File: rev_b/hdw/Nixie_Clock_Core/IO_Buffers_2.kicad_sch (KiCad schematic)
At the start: 15 parts

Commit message: hid all passive refdes on core PCB
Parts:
- C? (x2): Digi-Key PN (none) -> 1276-2970-1-ND
- C? (x3): Digi-Key PN (none) -> 1276-1935-1-ND
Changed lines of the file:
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@@
       (effects (font (size 1.27 1.27)) (justify right))
     )
-    (property "Digi-Key PN" "" (at 6.35 151.384 0)
+    (property "Digi-Key PN" "1276-2970-1-ND" (at 6.35 151.384 0)
       (effects (font (size 1.27 1.27)) hide)
     )
@@
       (effects (font (size 1.27 1.27)) (justify right))
     )
-    (property "Digi-Key PN" "" (at 149.225 22.86 0)
+    (property "Digi-Key PN" "1276-1935-1-ND" (at 149.225 22.86 0)
       (effects (font (size 1.524 1.524)) hide)
     )
@@
       (effects (font (size 1.27 1.27)) (justify right))
     )
-    (property "Digi-Key PN" "" (at 113.665 22.86 0)
+    (property "Digi-Key PN" "1276-1935-1-ND" (at 113.665 22.86 0)
       (effects (font (size 1.524 1.524)) hide)
     )
@@
       (effects (font (size 1.27 1.27)) (justify right))
     )
-    (property "Digi-Key PN" "" (at 64.135 128.27 0)
+    (property "Digi-Key PN" "1276-1935-1-ND" (at 64.135 128.27 0)
       (effects (font (size 1.524 1.524)) hide)
     )
@@
       (effects (font (size 1.27 1.27)) (justify right))
     )
-    (property "Digi-Key PN" "" (at -29.21 151.384 0)
-      (effects (font (size 1.27 1.27)) hide)
-    )
+    (property "Digi-Key PN" "1276-2970-1-ND" (at -29.21 151.384 0)
+      (effects (font (size 1.27 1.27)) hide)
+    )

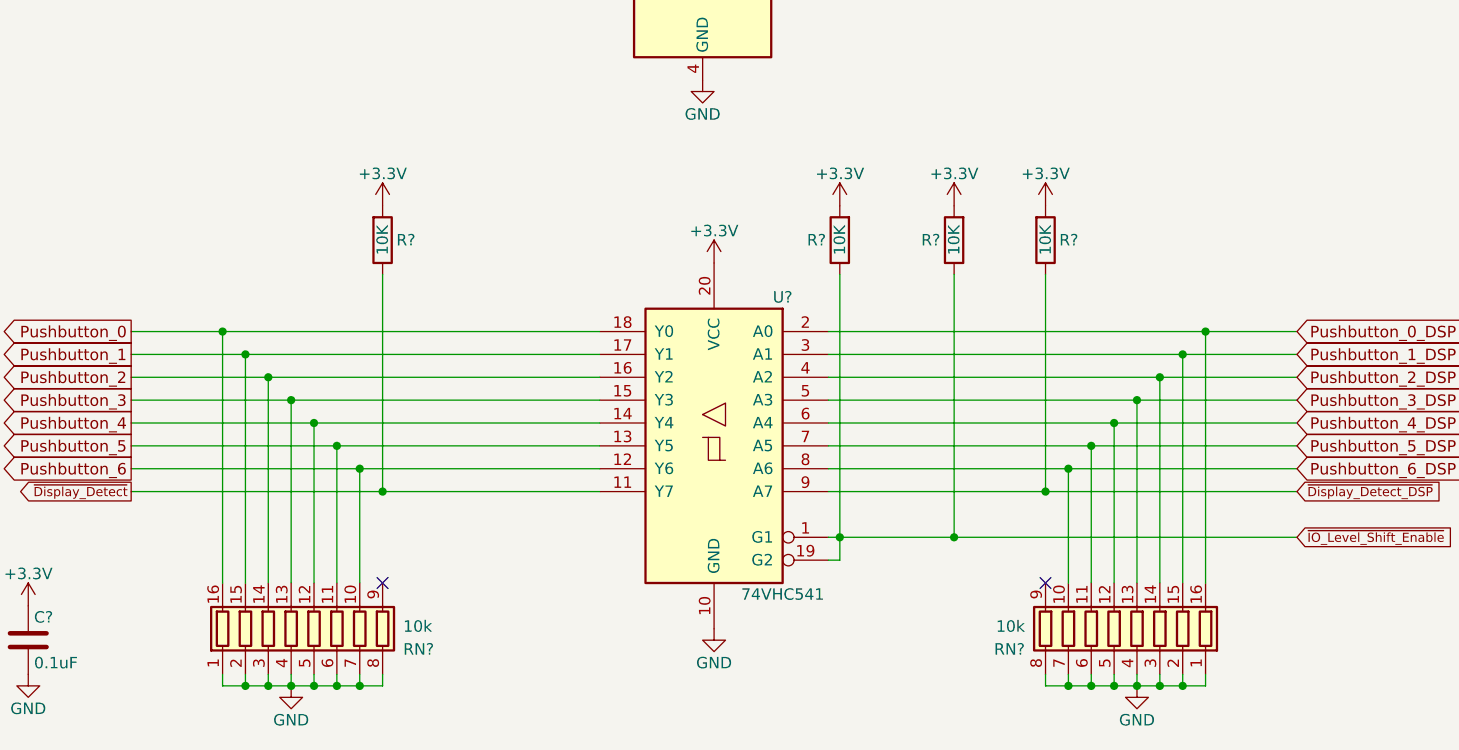
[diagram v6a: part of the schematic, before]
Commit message: much more component placement on core board
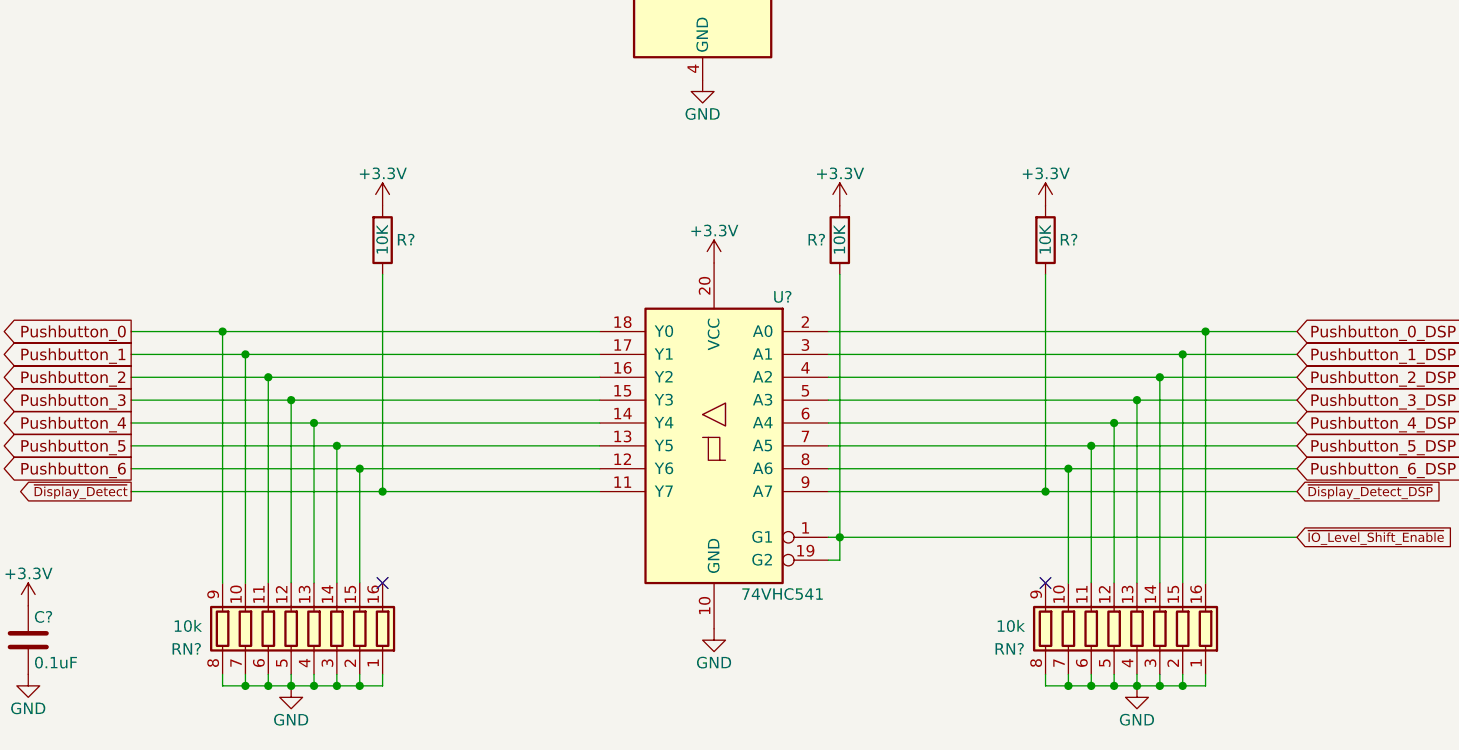
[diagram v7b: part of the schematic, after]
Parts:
- removed R?: 10K, Resistors_SMD:R_0603, symbol Custom_Library:R_Custom
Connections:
- net Pushbutton_0: now also RN?.9 (R8.2); no longer RN?.16 (R1.2)
- net Pushbutton_1: now also RN?.10 (R7.2); no longer RN?.15 (R2.2)
- net Pushbutton_2: now also RN?.11 (R6.2); no longer RN?.14 (R3.2)
- net Pushbutton_3: now also RN?.12 (R5.2); no longer RN?.13 (R4.2)
- net Pushbutton_4: now also RN?.13 (R4.2); no longer RN?.12 (R5.2)
- net Pushbutton_5: now also RN?.14 (R3.2); no longer RN?.11 (R6.2)
- net Pushbutton_6: now also RN?.15 (R2.2); no longer RN?.10 (R7.2)
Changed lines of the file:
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@@
   (junction (at 74.93 106.68) (diameter 0) (color 0 0 0 0)
-  )
-  (junction (at 156.21 129.54) (diameter 0) (color 0 0 0 0)
   )
   (junction (at 77.47 146.05) (diameter 0) (color 0 0 0 0)
@@
     (stroke (width 0) (type default))
   )
-  (wire (pts (xy 156.21 129.54) (xy 194.31 129.54))
+  (wire (pts (xy 143.51 129.54) (xy 194.31 129.54))
     (stroke (width 0) (type default))
   )
@@
     (stroke (width 0) (type default))
   )
-  (wire (pts (xy 156.21 129.54) (xy 143.51 129.54))
-    (stroke (width 0) (type default))
-  )
   (wire (pts (xy 176.53 144.78) (xy 176.53 146.05))
     (stroke (width 0) (type default))
@@
   )
   (wire (pts (xy 168.91 144.78) (xy 168.91 146.05))
-    (stroke (width 0) (type default))
-  )
-  (wire (pts (xy 156.21 129.54) (xy 156.21 100.33))
     (stroke (width 0) (type default))
   )
@@
         (path "/16fdce21-b570-4d81-a458-e8839d611806/8bfc37a9-2570-4706-99e7-147636a5a42e"
           (reference "#PWR01822") (unit 1)
-        )
-      )
-    )
-  )
-  (symbol (lib_id "Custom_Library:R_Custom") (at 156.21 96.52 0) (unit 1)
-    (in_bom yes) (on_board yes) (dnp no)
-    (property "Reference" "R?" (at 154.686 96.52 0)
-      (effects (font (size 1.27 1.27)) (justify right))
-    )
-    (property "Value" "10K" (at 156.21 96.52 90)
-      (effects (font (size 1.27 1.27)))
-    )
-    (property "Footprint" "Resistors_SMD:R_0603" (at 156.21 96.52 0)
-      (effects (font (size 1.27 1.27)) hide)
-    )
-    (property "Datasheet" "" (at 156.21 96.52 0)
-      (effects (font (size 1.27 1.27)) hide)
-    )
-    (property "display_footprint" "0603" (at 157.988 94.234 0)
-      (effects (font (size 1.27 1.27)) (justify left) hide)
-    )
-    (property "Tolerance" "1%" (at 157.988 96.52 0)
-      (effects (font (size 1.27 1.27)) (justify left) hide)
-    )
-    (property "Wattage" "1/10W" (at 157.988 98.552 0)
-      (effects (font (size 1.27 1.27)) (justify left) hide)
-    )
-    (property "Digi-Key PN" "" (at 163.83 86.36 0)
-      (effects (font (size 1.524 1.524)) hide)
-    )
-    (pin "1")
-    (pin "2")
-    (instances
-      (project "VFD_Clock"
-        (path "/0e0fa043-3ab8-4cb9-8105-f968ef03a597/00000000-0000-0000-0000-00005bb6cf6d"
-          (reference "R?") (unit 1)
-        )
-        (path "/0e0fa043-3ab8-4cb9-8105-f968ef03a597/00000000-0000-0000-0000-00005cb8a16a"
-          (reference "R?") (unit 1)
-        )
-        (path "/0e0fa043-3ab8-4cb9-8105-f968ef03a597/00000000-0000-0000-0000-00005baae2b6"
-          (reference "R?") (unit 1)
-        )
-        (path "/0e0fa043-3ab8-4cb9-8105-f968ef03a597/00000000-0000-0000-0000-00005cc31b3e"
-          (reference "R?") (unit 1)
-        )
-        (path "/0e0fa043-3ab8-4cb9-8105-f968ef03a597/00000000-0000-0000-0000-00005bbe424c"
-          (reference "R?") (unit 1)
-        )
-      )
-      (project "Nixie_Clock_Core"
-        (path "/16fdce21-b570-4d81-a458-e8839d611806/8bfc37a9-2570-4706-99e7-147636a5a42e"
-          (reference "R1804") (unit 1)
         )
       )
@@
     )
   )
-  (symbol (lib_id "Device:R_Pack08") (at 85.09 139.7 0) (unit 1)
-    (in_bom yes) (on_board yes) (dnp no)
-    (property "Reference" "RN?" (at 94.996 141.986 0)
+  (symbol (lib_id "Device:R_Pack08") (at 82.55 139.7 0) (mirror y) (unit 1)
+    (in_bom yes) (on_board yes) (dnp no)
+    (property "Reference" "RN?" (at 72.644 141.986 0)
       (effects (font (size 1.27 1.27)) (justify left))
     )
-    (property "Value" "10k" (at 94.996 139.446 0)
+    (property "Value" "10k" (at 72.644 139.446 0)
       (effects (font (size 1.27 1.27)) (justify left))
     )
-    (property "Footprint" "Resistors_SMD:R_Array_Convex_8x0602" (at 97.155 139.7 90)
-      (effects (font (size 1.27 1.27)) hide)
-    )
-    (property "Datasheet" "~" (at 85.09 139.7 0)
-      (effects (font (size 1.27 1.27)) hide)
-    )
-    (property "Digi-Key PN" "Y1103CT-ND" (at 85.09 139.7 0)
+    (property "Footprint" "Resistors_SMD:R_Array_Convex_8x0602" (at 70.485 139.7 90)
+      (effects (font (size 1.27 1.27)) hide)
+    )
+    (property "Datasheet" "~" (at 82.55 139.7 0)
+      (effects (font (size 1.27 1.27)) hide)
+    )
+    (property "Digi-Key PN" "Y1103CT-ND" (at 82.55 139.7 0)
       (effects (font (size 1.27 1.27)) hide)
     )
@@
         )
       )
-    )
-  )
-  (symbol (lib_id "power:+3.3V") (at 156.21 92.71 0) (mirror y) (unit 1)
-    (in_bom yes) (on_board yes) (dnp no)
-    (property "Reference" "#PWR?" (at 156.21 96.52 0)
-      (effects (font (size 1.27 1.27)) hide)
-    )
-    (property "Value" "+3.3V" (at 156.21 89.154 0)
-      (effects (font (size 1.27 1.27)))
-    )
-    (property "Footprint" "" (at 156.21 92.71 0)
-      (effects (font (size 1.27 1.27)) hide)
-    )
-    (property "Datasheet" "" (at 156.21 92.71 0)
-      (effects (font (size 1.27 1.27)) hide)
-    )
-    (pin "1")
-    (instances
-      (project "VFD_Clock"
-        (path "/0e0fa043-3ab8-4cb9-8105-f968ef03a597/00000000-0000-0000-0000-00005bb6cf6d"
-          (reference "#PWR?") (unit 1)
-        )
-        (path "/0e0fa043-3ab8-4cb9-8105-f968ef03a597/00000000-0000-0000-0000-00005cb8a16a"
-          (reference "#PWR?") (unit 1)
-        )
-        (path "/0e0fa043-3ab8-4cb9-8105-f968ef03a597/00000000-0000-0000-0000-00005baae2b6"
-          (reference "#PWR?") (unit 1)
-        )
-        (path "/0e0fa043-3ab8-4cb9-8105-f968ef03a597/00000000-0000-0000-0000-00005cc31b3e"
-          (reference "#PWR?") (unit 1)
-        )
-        (path "/0e0fa043-3ab8-4cb9-8105-f968ef03a597/00000000-0000-0000-0000-00005bbe424c"
-          (reference "#PWR?") (unit 1)
-        )
-      )
-      (project "Nixie_Clock_Core"
-        (path "/16fdce21-b570-4d81-a458-e8839d611806/8bfc37a9-2570-4706-99e7-147636a5a42e"
-          (reference "#PWR01804") (unit 1)
-        )
-      )

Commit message: lots more PCB placement
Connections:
- net Pushbutton_0: now also R?.2, U?.11 (Y7); no longer RN?.9 (R8.2), U?.18 (Y0)
- net Pushbutton_0_DSP: now also R?.2, U?.9 (A7); no longer RN?.16 (R1.2), U?.2 (A0)
- net Pushbutton_1: now also RN?.15 (R2.2), U?.12 (Y6); no longer RN?.10 (R7.2), U?.17 (Y1)
- net Pushbutton_1_DSP: now also RN?.10 (R7.2), U?.8 (A6); no longer RN?.15 (R2.2), U?.3 (A1)
- net Pushbutton_2: now also RN?.14 (R3.2), U?.13 (Y5); no longer RN?.11 (R6.2), U?.16 (Y2)
- net Pushbutton_2_DSP: now also RN?.11 (R6.2), U?.7 (A5); no longer RN?.14 (R3.2), U?.4 (A2)
- net Pushbutton_3: now also RN?.13 (R4.2), U?.14 (Y4); no longer RN?.12 (R5.2), U?.15 (Y3)
- net Pushbutton_3_DSP: now also RN?.12 (R5.2), U?.6 (A4); no longer RN?.13 (R4.2), U?.5 (A3)
- net Pushbutton_4: now also RN?.12 (R5.2), U?.15 (Y3); no longer RN?.13 (R4.2), U?.14 (Y4)
- net Pushbutton_4_DSP: now also RN?.13 (R4.2), U?.5 (A3); no longer RN?.12 (R5.2), U?.6 (A4)
- net Pushbutton_5: now also RN?.11 (R6.2), U?.16 (Y2); no longer RN?.14 (R3.2), U?.13 (Y5)
- net Pushbutton_5_DSP: now also RN?.14 (R3.2), U?.4 (A2); no longer RN?.11 (R6.2), U?.7 (A5)
- net Pushbutton_6: now also RN?.10 (R7.2), U?.17 (Y1); no longer RN?.15 (R2.2), U?.12 (Y6)
- net Pushbutton_6_DSP: now also RN?.15 (R2.2), U?.3 (A1); no longer RN?.10 (R7.2), U?.8 (A6)
- net ~{Display_Detect_DSP}: now also RN?.16 (R1.2), U?.2 (A0); no longer R?.2, U?.9 (A7)
- net ~{Display_Detect}: now also RN?.9 (R8.2), U?.18 (Y0); no longer R?.2, U?.11 (Y7)
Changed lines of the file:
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@@
     (effects (font (face "Courier New") (size 5.08 5.08) (thickness 0.254) bold (color 255 37 56 1)) (justify left bottom))
   )
-  (global_label "Pushbutton_2" (shape output) (at 64.77 111.76 180) (fields_autoplaced)
+  (global_label "Pushbutton_2" (shape output) (at 64.77 119.38 180) (fields_autoplaced)
+    (effects (font (size 1.27 1.27)) (justify right))
+    (property "Intersheetrefs" "${INTERSHEET_REFS}" (at 49.0436 119.38 0)
+      (effects (font (size 1.27 1.27)) (justify right) hide)
+    )
+  )
+  (global_label "Pushbutton_5" (shape output) (at 64.77 111.76 180) (fields_autoplaced)
     (effects (font (size 1.27 1.27)) (justify right))
     (property "Intersheetrefs" "${INTERSHEET_REFS}" (at 49.0436 111.76 0)
@@
     )
   )
-  (global_label "Pushbutton_5" (shape output) (at 64.77 119.38 180) (fields_autoplaced)
-    (effects (font (size 1.27 1.27)) (justify right))
-    (property "Intersheetrefs" "${INTERSHEET_REFS}" (at 49.0436 119.38 0)
-      (effects (font (size 1.27 1.27)) (justify right) hide)
-    )
-  )
-  (global_label "~{Display_Detect_DSP}" (shape input) (at 194.31 124.46 0)
+  (global_label "~{Display_Detect_DSP}" (shape input) (at 194.31 106.68 0)
     (effects (font (size 1.016 1.016)) (justify left))
-    (property "Intersheetrefs" "${INTERSHEET_REFS}" (at 194.31 124.46 0)
+    (property "Intersheetrefs" "${INTERSHEET_REFS}" (at 194.31 106.68 0)
       (effects (font (size 1.27 1.27)) hide)
     )
   )
-  (global_label "Pushbutton_6_DSP" (shape input) (at 194.31 121.92 0) (fields_autoplaced)
+  (global_label "Pushbutton_6_DSP" (shape input) (at 194.31 109.22 0) (fields_autoplaced)
     (effects (font (size 1.27 1.27)) (justify left))
-    (property "Intersheetrefs" "${INTERSHEET_REFS}" (at 214.7535 121.92 0)
+    (property "Intersheetrefs" "${INTERSHEET_REFS}" (at 214.7535 109.22 0)
       (effects (font (size 1.27 1.27)) (justify left) hide)
     )
@@
     )
   )
-  (global_label "Pushbutton_6" (shape output) (at 64.77 121.92 180) (fields_autoplaced)
+  (global_label "Pushbutton_6" (shape output) (at 64.77 109.22 180) (fields_autoplaced)
     (effects (font (size 1.27 1.27)) (justify right))
-    (property "Intersheetrefs" "${INTERSHEET_REFS}" (at 49.0436 121.92 0)
+    (property "Intersheetrefs" "${INTERSHEET_REFS}" (at 49.0436 109.22 0)
       (effects (font (size 1.27 1.27)) (justify right) hide)
     )
   )
-  (global_label "Pushbutton_2_DSP" (shape input) (at 194.31 111.76 0) (fields_autoplaced)
+  (global_label "Pushbutton_2_DSP" (shape input) (at 194.31 119.38 0) (fields_autoplaced)
     (effects (font (size 1.27 1.27)) (justify left))
-    (property "Intersheetrefs" "${INTERSHEET_REFS}" (at 214.7535 111.76 0)
+    (property "Intersheetrefs" "${INTERSHEET_REFS}" (at 214.7535 119.38 0)
       (effects (font (size 1.27 1.27)) (justify left) hide)
     )
   )
-  (global_label "~{Display_Detect}" (shape output) (at 64.77 124.46 180)
+  (global_label "~{Display_Detect}" (shape output) (at 64.77 106.68 180)
     (effects (font (size 1.016 1.016)) (justify right))
-    (property "Intersheetrefs" "${INTERSHEET_REFS}" (at 64.77 124.46 0)
+    (property "Intersheetrefs" "${INTERSHEET_REFS}" (at 64.77 106.68 0)
       (effects (font (size 1.27 1.27)) hide)
     )
@@
     )
   )
-  (global_label "Pushbutton_4" (shape output) (at 64.77 116.84 180) (fields_autoplaced)
+  (global_label "Pushbutton_4" (shape output) (at 64.77 114.3 180) (fields_autoplaced)
     (effects (font (size 1.27 1.27)) (justify right))
-    (property "Intersheetrefs" "${INTERSHEET_REFS}" (at 49.0436 116.84 0)
+    (property "Intersheetrefs" "${INTERSHEET_REFS}" (at 49.0436 114.3 0)
       (effects (font (size 1.27 1.27)) (justify right) hide)
     )
   )
-  (global_label "Pushbutton_0" (shape output) (at 64.77 106.68 180) (fields_autoplaced)
+  (global_label "Pushbutton_0" (shape output) (at 64.77 124.46 180) (fields_autoplaced)
     (effects (font (size 1.27 1.27)) (justify right))
-    (property "Intersheetrefs" "${INTERSHEET_REFS}" (at 49.0436 106.68 0)
+    (property "Intersheetrefs" "${INTERSHEET_REFS}" (at 49.0436 124.46 0)
       (effects (font (size 1.27 1.27)) (justify right) hide)
     )
   )
-  (global_label "Pushbutton_1" (shape output) (at 64.77 109.22 180) (fields_autoplaced)
+  (global_label "Pushbutton_1" (shape output) (at 64.77 121.92 180) (fields_autoplaced)
     (effects (font (size 1.27 1.27)) (justify right))
-    (property "Intersheetrefs" "${INTERSHEET_REFS}" (at 49.0436 109.22 0)
+    (property "Intersheetrefs" "${INTERSHEET_REFS}" (at 49.0436 121.92 0)
       (effects (font (size 1.27 1.27)) (justify right) hide)
     )
   )
-  (global_label "Pushbutton_3_DSP" (shape input) (at 194.31 114.3 0) (fields_autoplaced)
+  (global_label "Pushbutton_3_DSP" (shape input) (at 194.31 116.84 0) (fields_autoplaced)
     (effects (font (size 1.27 1.27)) (justify left))
-    (property "Intersheetrefs" "${INTERSHEET_REFS}" (at 214.7535 114.3 0)
+    (property "Intersheetrefs" "${INTERSHEET_REFS}" (at 214.7535 116.84 0)
       (effects (font (size 1.27 1.27)) (justify left) hide)
     )
@@
     )
   )
-  (global_label "Pushbutton_5_DSP" (shape input) (at 194.31 119.38 0) (fields_autoplaced)
+  (global_label "Pushbutton_5_DSP" (shape input) (at 194.31 111.76 0) (fields_autoplaced)
     (effects (font (size 1.27 1.27)) (justify left))
-    (property "Intersheetrefs" "${INTERSHEET_REFS}" (at 214.7535 119.38 0)
+    (property "Intersheetrefs" "${INTERSHEET_REFS}" (at 214.7535 111.76 0)
       (effects (font (size 1.27 1.27)) (justify left) hide)
     )
@@
     )
   )
-  (global_label "Pushbutton_4_DSP" (shape input) (at 194.31 116.84 0) (fields_autoplaced)
+  (global_label "Pushbutton_4_DSP" (shape input) (at 194.31 114.3 0) (fields_autoplaced)
     (effects (font (size 1.27 1.27)) (justify left))
-    (property "Intersheetrefs" "${INTERSHEET_REFS}" (at 214.7535 116.84 0)
+    (property "Intersheetrefs" "${INTERSHEET_REFS}" (at 214.7535 114.3 0)
       (effects (font (size 1.27 1.27)) (justify left) hide)
     )
   )
-  (global_label "Pushbutton_1_DSP" (shape input) (at 194.31 109.22 0) (fields_autoplaced)
+  (global_label "Pushbutton_1_DSP" (shape input) (at 194.31 121.92 0) (fields_autoplaced)
     (effects (font (size 1.27 1.27)) (justify left))
-    (property "Intersheetrefs" "${INTERSHEET_REFS}" (at 214.7535 109.22 0)
+    (property "Intersheetrefs" "${INTERSHEET_REFS}" (at 214.7535 121.92 0)
       (effects (font (size 1.27 1.27)) (justify left) hide)
     )
   )
-  (global_label "Pushbutton_0_DSP" (shape input) (at 194.31 106.68 0) (fields_autoplaced)
+  (global_label "Pushbutton_0_DSP" (shape input) (at 194.31 124.46 0) (fields_autoplaced)
     (effects (font (size 1.27 1.27)) (justify left))
-    (property "Intersheetrefs" "${INTERSHEET_REFS}" (at 214.7535 106.68 0)
+    (property "Intersheetrefs" "${INTERSHEET_REFS}" (at 214.7535 124.46 0)
       (effects (font (size 1.27 1.27)) (justify left) hide)
     )
   )
-  (global_label "Pushbutton_3" (shape output) (at 64.77 114.3 180) (fields_autoplaced)
+  (global_label "Pushbutton_3" (shape output) (at 64.77 116.84 180) (fields_autoplaced)
     (effects (font (size 1.27 1.27)) (justify right))
-    (property "Intersheetrefs" "${INTERSHEET_REFS}" (at 49.0436 114.3 0)
+    (property "Intersheetrefs" "${INTERSHEET_REFS}" (at 49.0436 116.84 0)
       (effects (font (size 1.27 1.27)) (justify right) hide)
     )
